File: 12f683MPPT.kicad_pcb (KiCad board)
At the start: 2 copper layers, 98.3 x 72.6 mm, 53 parts, among them Q1 BUK9511-55A127, Q2 BUK9511-55A127, Q3 2N2222A, Q4 2N2222A, Q5 2N2907A, SW1 SW_Push, U1 LM7805_TO220, U2 PIC12F683-IP, U3 LM358

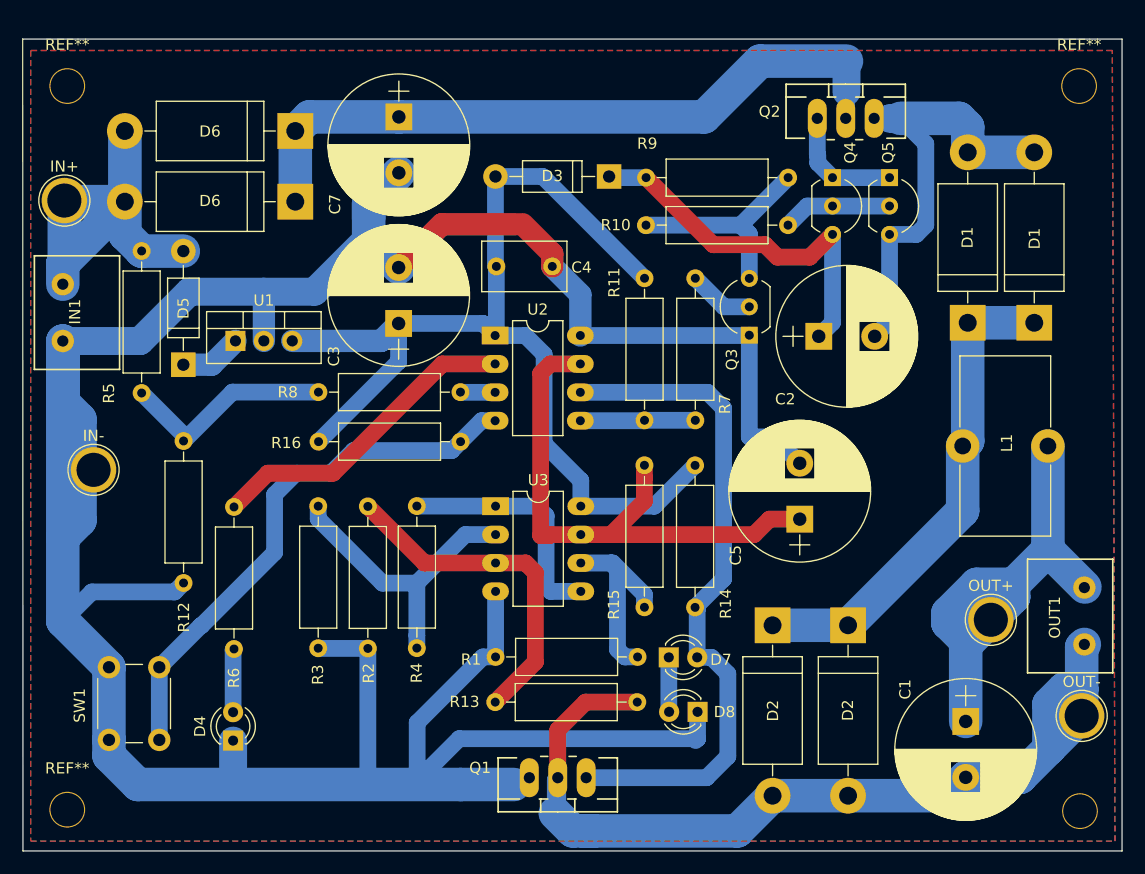
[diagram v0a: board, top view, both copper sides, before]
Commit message: Add zener diode for FET protection.
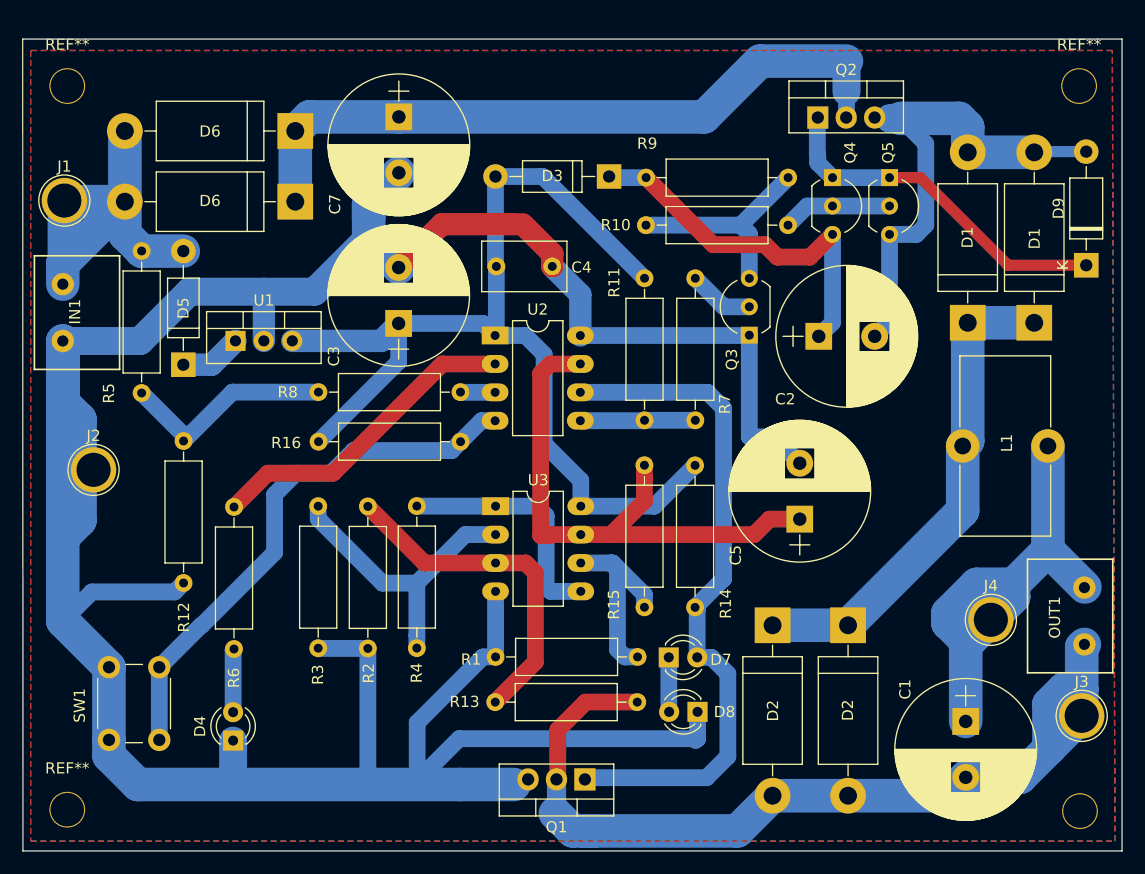
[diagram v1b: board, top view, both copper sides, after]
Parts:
- added D9: 1N5733A 5.1V, Diode_THT:D_DO-41_SOD81_P10.16mm_Horizontal, F.Cu at (131.3, 46.7)
- Q1, Q2: footprint TO_SOT_Packages_THT-2:TO-220_Neutral123_Vertical_LargePads -> Package_TO_SOT_THT:TO-220-3_Vertical
- moved Q2 2.50 mm to (107.3, 33.5)
- moved Q1 2.43 mm to (86.5, 92.7)
- renumbered IN+ to J1, IN- to J2, OUT- to J3, OUT+ to J4
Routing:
- net Net-(D9-Pad1): track 11.0 -> 31.8 mm
- net Net-(C2-Pad2): track 40.7 -> 45.4 mm

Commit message: R9 -> 2.2k
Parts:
- R9: value 10k -> 2.2k

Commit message: Update PCB.
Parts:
- removed the REF** at (40.2, 95.4)
- removed the REF** at (40.2, 30.7)
- removed the REF** at (130.7, 30.7)
- removed the REF** at (130.8, 95.5)
- added REF**: MountingHole_3.2mm_M3_Pad, MountingHole:MountingHole_3.2mm_M3_Pad, F.Cu at (39.9, 30.3)
- added REF**: MountingHole_3.2mm_M3_Pad, MountingHole:MountingHole_3.2mm_M3_Pad, F.Cu at (40.1, 95.2)
- added REF**: MountingHole_3.2mm_M3_Pad, MountingHole:MountingHole_3.2mm_M3_Pad, F.Cu at (130.6, 95.3)
- added REF**: MountingHole_3.2mm_M3_Pad, MountingHole:MountingHole_3.2mm_M3_Pad, F.Cu at (130.7, 30.5)
- SW1: footprint Buttons_Switches_THT:SW_PUSH_6mm -> Button_Switch_THT:SW_PUSH_6mm_H7.3mm

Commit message: Update PCB.
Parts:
- C2: value 10u 50v -> 4.7u 50v
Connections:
- C2 pad 1: Net-(C2-Pad1) -> /BootStrap
- C3 pad 1: /BootStrap -> Net-(C3-Pad1)
- C4 pad 1: /BootStrap -> Net-(C3-Pad1)
- D3 pad 1: Net-(C2-Pad1) -> /BootStrap
- D3 pad 2: /BootStrap -> Net-(C7-Pad1)
- Q4 pad 3: Net-(C2-Pad1) -> /BootStrap
- R11 pad 1: /BootStrap -> Net-(C3-Pad1)
- R14 pad 1: /BootStrap -> Net-(C3-Pad1)
- R16 pad 2: /BootStrap -> Net-(C3-Pad1)
- R9 pad 1: Net-(C2-Pad1) -> /BootStrap
- U1 pad 3: /BootStrap -> Net-(C3-Pad1)
- U2 pad 1: /BootStrap -> Net-(C3-Pad1)
- U3 pad 8: /BootStrap -> Net-(C3-Pad1)
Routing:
- net Net-(C3-Pad1): track 0.00 -> 89.3 mm
- net /BootStrap: track 97.5 -> 33.4 mm
- net Net-(C2-Pad1): track 33.4 -> 0.00 mm
- net Net-(C7-Pad1): track 63.3 -> 74.2 mm

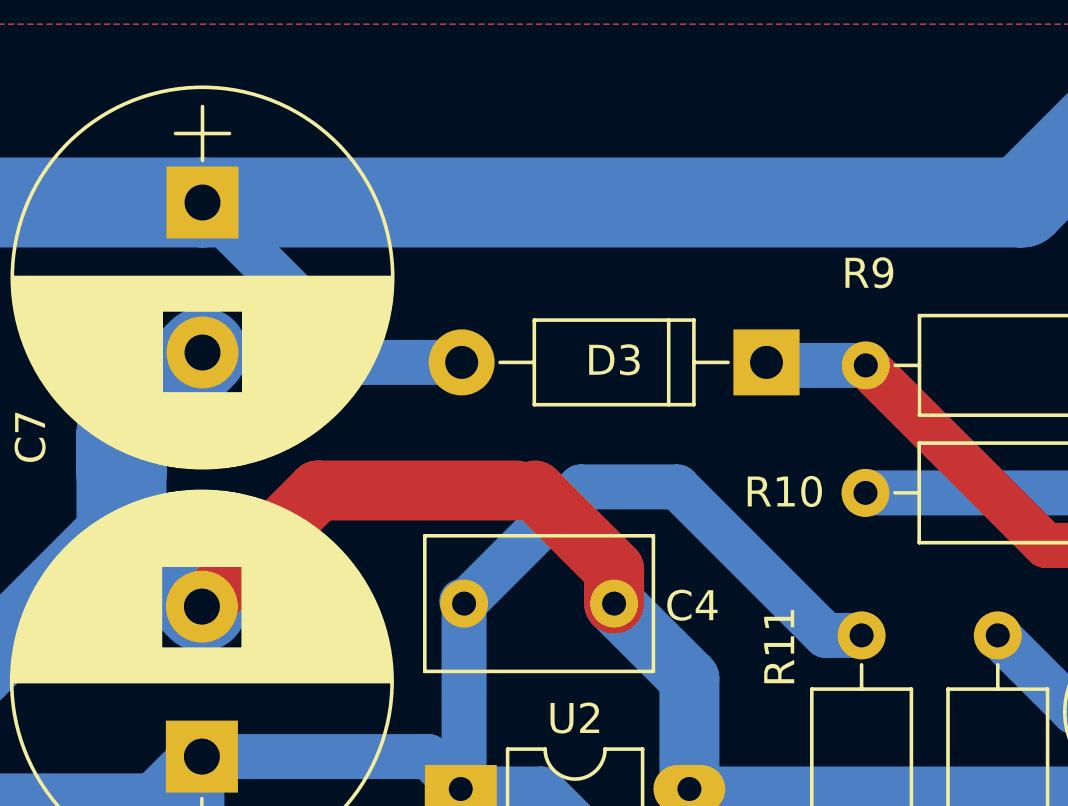
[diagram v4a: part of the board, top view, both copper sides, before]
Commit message: Revert and change Diode.
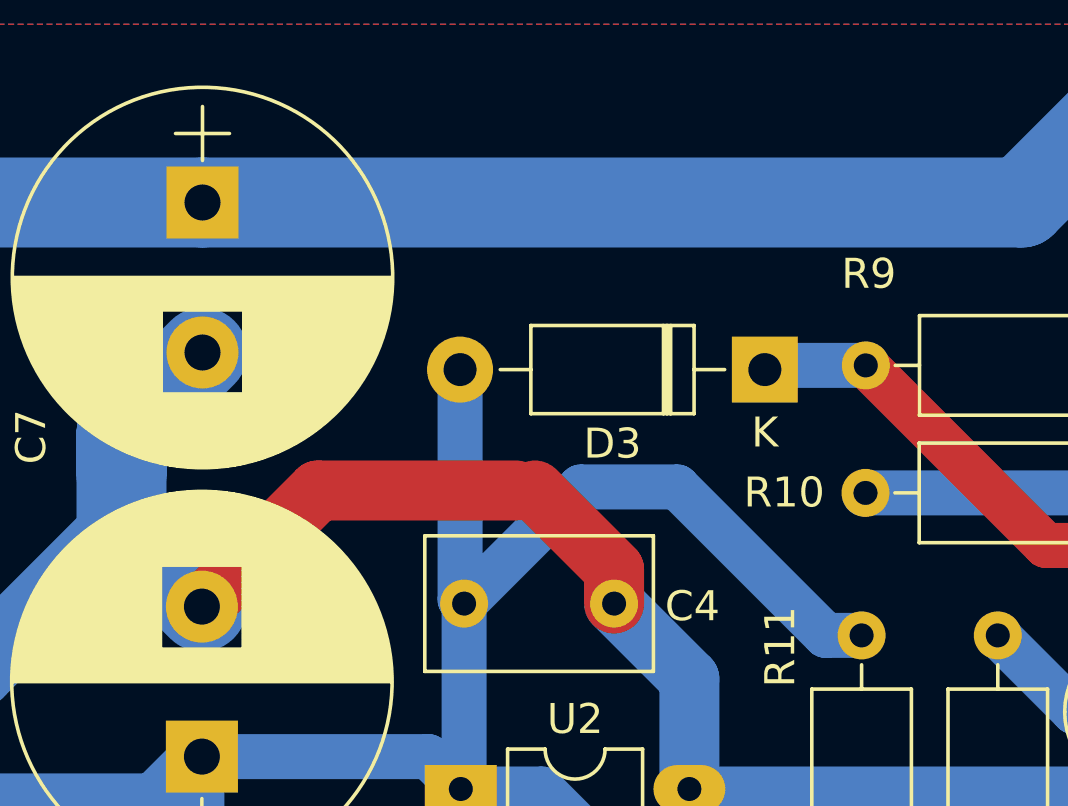
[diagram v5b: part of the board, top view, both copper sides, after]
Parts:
- D3: value 1N4148 -> 1N5819; footprint Diodes_THT:D_DO-41_SOD81_P10.16mm_Horizontal -> Diode_THT:D_DO-41_SOD81_P10.16mm_Horizontal
- moved D3 0.25 mm to (88.6, 39.0)
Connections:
- D3 pad 2: Net-(C7-Pad1) -> Net-(C3-Pad1)
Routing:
- net Net-(C7-Pad1): track 74.2 -> 63.3 mm
- net Net-(C3-Pad1): track 89.3 -> 97.2 mm

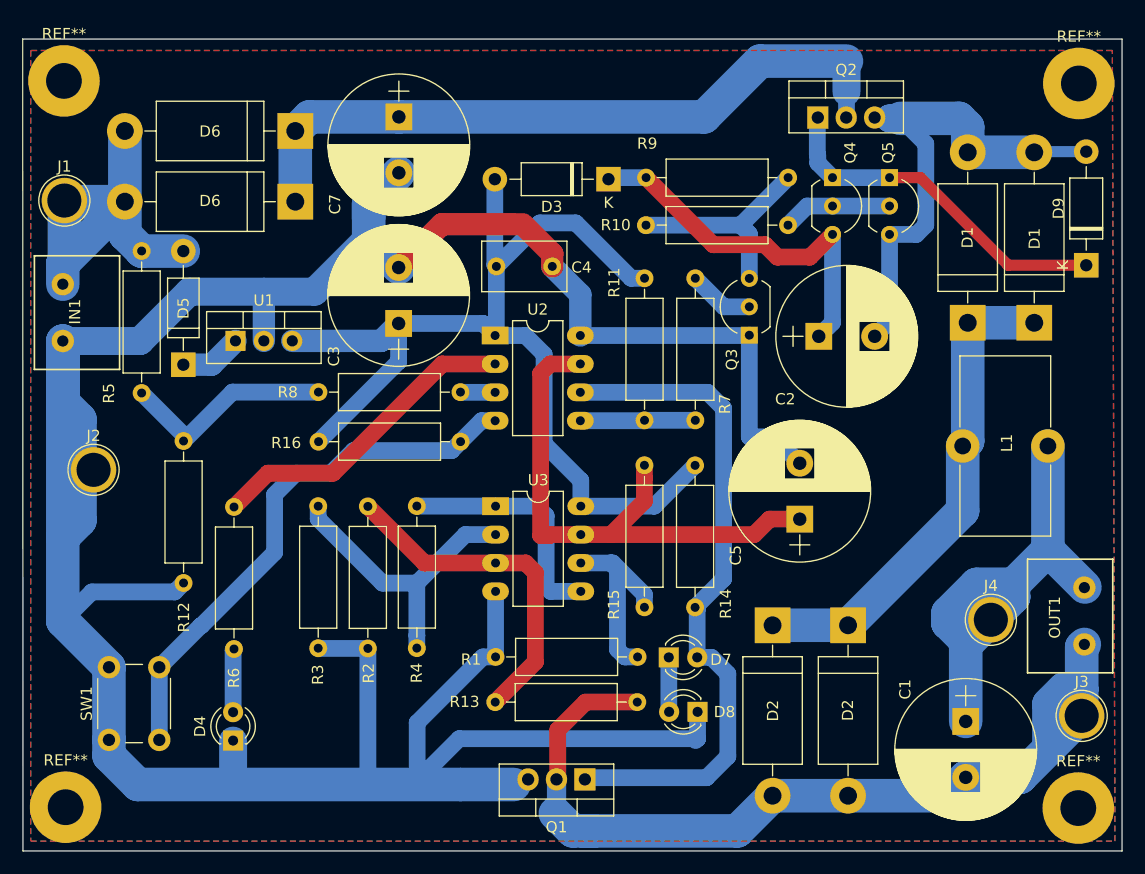
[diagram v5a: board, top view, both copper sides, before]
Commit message: Fix circuit. R1 -> 1k ohm.
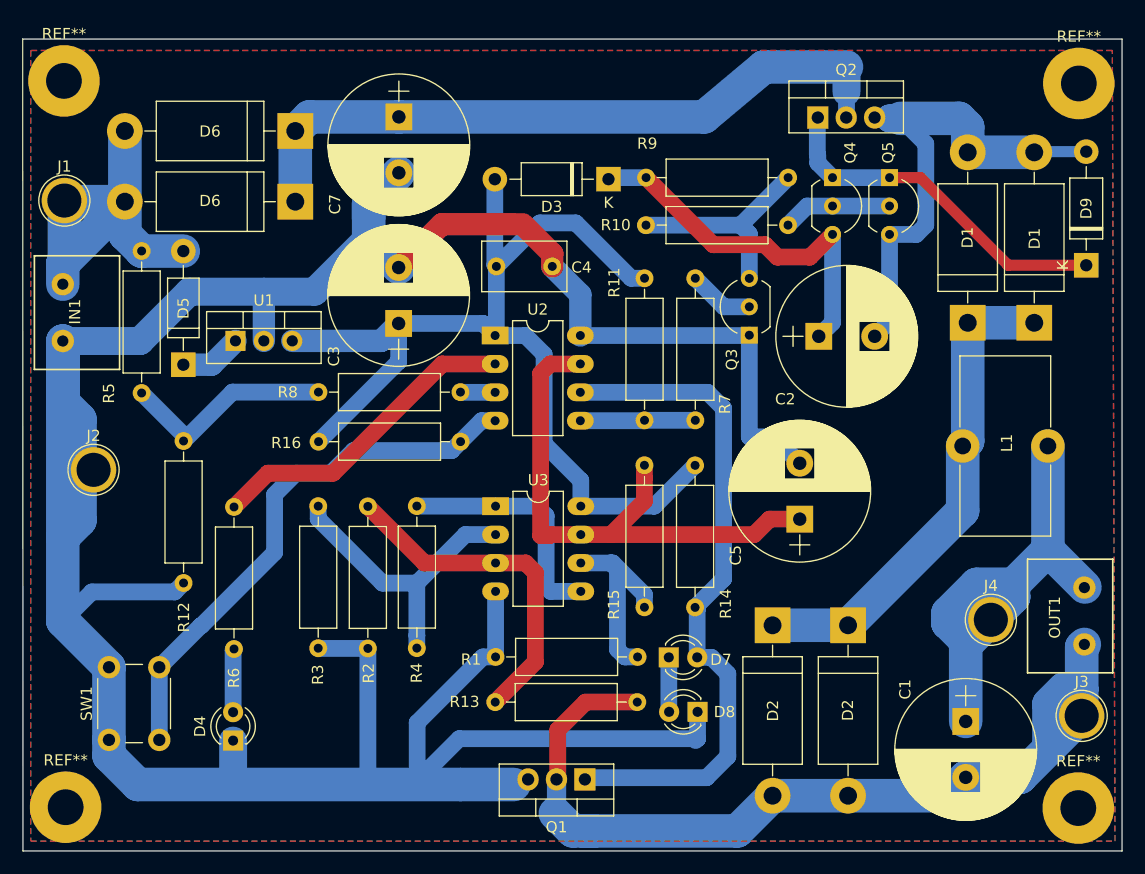
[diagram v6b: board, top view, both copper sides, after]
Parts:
- R1: value 10k -> 1k
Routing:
- net Net-(D6-K): track 63.3 -> 62.4 mm
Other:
- net class Default removed
